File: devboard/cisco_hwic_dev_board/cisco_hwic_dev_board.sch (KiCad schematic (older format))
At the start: 3 parts, among them J1 Conn_02x20_Odd_Even, J2 Conn_02x34_Top_Bottom_Cisco, J3 Conn_01x15

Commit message: Expansion connector routed.
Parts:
- J3: footprint Connector_PinHeader_2.54mm:PinHeader_1x15_P2.54mm_Vertical -> cisco_hwic_dev_board:PinHeader_1x15_P2.54mm_Vertical_Cisco; symbol Connector_Generic:Conn_01x15 -> cisco_hwic_dev_board:Conn_01x15_Cisco
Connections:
- net labels added: PC2
- wire segments 99 -> 114
- no-connect marks 11 -> 2
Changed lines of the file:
@@
 	4400 6700 4050 6700
 Wire Wire Line
-	4400 6600 4050 6600
+	4400 6500 4050 6500
 $Comp
 L power:+5V #PWR02
 U 1 1 5DE56489
-P 4050 6600
-F 0 "#PWR02" H 4050 6450 50  0001 C CNN
-F 1 "+5V" V 4050 6800 50  0000 C CNN
-F 2 "" H 4050 6600 50  0001 C CNN
-F 3 "" H 4050 6600 50  0001 C CNN
-	1    4050 6600
+P 4050 6500
+F 0 "#PWR02" H 4050 6350 50  0001 C CNN
+F 1 "+5V" V 4050 6700 50  0000 C CNN
+F 2 "" H 4050 6500 50  0001 C CNN
+F 3 "" H 4050 6500 50  0001 C CNN
+	1    4050 6500
 	0    -1   -1   0
 $EndComp
@@
 Pin_32
 $Comp
-L Connector_Generic:Conn_01x15 J3
+L cisco_hwic_dev_board:Conn_01x15_Cisco J3
 U 1 1 5DE57370
 P 4600 6200
 F 0 "J3" H 4550 7050 50  0000 L CNN
 F 1 "Conn_01x15" H 4350 5400 50  0000 L CNN
-F 2 "Connector_PinHeader_2.54mm:PinHeader_1x15_P2.54mm_Vertical" H 4600 6200 50  0001 C CNN
+F 2 "cisco_hwic_dev_board:PinHeader_1x15_P2.54mm_Vertical_Cisco" H 4600 6200 50  0001 C CNN
 F 3 "~" H 4600 6200 50  0001 C CNN
 	1    4600 6200
@@
 	4150 5150 5000 5150
 Wire Wire Line
-	4150 5150 4150 6800
+	4150 5150 4150 6600
 Text Label 3000 2650 2    50   ~ 0
 DATA0
@@
 Wire Wire Line
 	5000 1750 5000 1850
-Wire Wire Line
-	4850 3150 5300 3150
 Text Label 5150 3150 0    50   ~ 0
 Pin_50
@@
 NoConn ~ 4400 5500
 NoConn ~ 4400 5600
-NoConn ~ 4400 5700
-NoConn ~ 4400 5800
-NoConn ~ 4400 5900
-NoConn ~ 4400 6000
-NoConn ~ 4400 6100
-NoConn ~ 4400 6200
-NoConn ~ 4400 6300
-NoConn ~ 4400 6400
-NoConn ~ 4400 6500
 Wire Wire Line
 	3400 1850 4350 1850
@@
 PA0
 Wire Wire Line
-	7650 1600 8600 1600
-Text Label 8250 1600 2    50   ~ 0
+	9100 1500 10050 1500
+Text Label 9700 1500 2    50   ~ 0
 PA1
+Wire Wire Line
+	9100 1600 10050 1600
 Text Label 8250 1700 2    50   ~ 0
-PB0
+PB2
 Wire Wire Line
 	7650 1700 8600 1700
+Text Label 9700 1700 2    50   ~ 0
+PB3
+Wire Wire Line
+	9100 1700 10050 1700
 Text Label 8250 1800 2    50   ~ 0
-PB1
+PB4
 Wire Wire Line
 	7650 1800 8600 1800
+Text Label 9700 1800 2    50   ~ 0
+PB5
+Wire Wire Line
+	9100 1800 10050 1800
 Text Label 8250 1900 2    50   ~ 0
-PB2
+PB6
 Wire Wire Line
 	7650 1900 8600 1900
+Text Label 9700 1900 2    50   ~ 0
+PB7
+Wire Wire Line
+	9100 1900 10050 1900
 Text Label 8250 2000 2    50   ~ 0
-PB3
+PB8
 Wire Wire Line
 	7650 2000 8600 2000
-Text Label 8250 2100 2    50   ~ 0
-PB4
+Wire Wire Line
+	7650 2300 8600 2300
+Text Label 8250 2300 2    50   ~ 0
+PD0
+Text Label 9700 2300 2    50   ~ 0
+PD1
+Wire Wire Line
+	7650 2400 8600 2400
+Text Label 8250 2400 2    50   ~ 0
+PD2
+Text Label 9700 2400 2    50   ~ 0
+PD3
+Wire Wire Line
+	7650 2500 8600 2500
+Text Label 8250 2500 2    50   ~ 0
+PD4
+Text Label 9700 2500 2    50   ~ 0
+PD5
+Wire Wire Line
+	7650 2600 8600 2600
+Text Label 8250 2600 2    50   ~ 0
+PD6
+Text Label 9700 2600 2    50   ~ 0
+PD7
 Wire Wire Line
 	7650 2100 8600 2100
-Text Label 8250 2200 2    50   ~ 0
-PB5
-Wire Wire Line
-	7650 2200 8600 2200
-Text Label 8250 2300 2    50   ~ 0
-PB6
-Wire Wire Line
-	7650 2300 8600 2300
-Text Label 8250 2400 2    50   ~ 0
-PB7
-Wire Wire Line
-	7650 2400 8600 2400
-Text Label 8250 2500 2    50   ~ 0
-PB8
-Wire Wire Line
-	7650 2500 8600 2500
+Text Label 8100 2100 0    50   ~ 0
+PC0
+Wire Wire Line
+	9100 2100 10050 2100
+Text Label 9550 2100 0    50   ~ 0
+PC1
+Wire Wire Line
+	7650 2800 8600 2800
+Text Label 8100 2800 0    50   ~ 0
+PG0
+Text Label 9550 2800 0    50   ~ 0
+PG1
+Wire Wire Line
+	7650 2900 8600 2900
+Text Label 8100 2900 0    50   ~ 0
+PG2
+Text Label 9550 2900 0    50   ~ 0
+PG3
+Wire Wire Line
+	7650 3000 8600 3000
+Text Label 8100 3000 0    50   ~ 0
+PG4
+Text Label 9550 3000 0    50   ~ 0
+PG5
+Wire Wire Line
+	7650 3100 8600 3100
+Text Label 8100 3100 0    50   ~ 0
+PG6
+Text Label 9550 3100 0    50   ~ 0
+PG7
+Text Label 8100 2700 0    50   ~ 0
+PE0
+Wire Wire Line
+	9100 2700 10050 2700
+Text Label 9550 2700 0    50   ~ 0
+PF0
+Wire Wire Line
+	7650 3200 8600 3200
+Text Label 8100 3200 0    50   ~ 0
+PH0
+Text Label 9550 3200 0    50   ~ 0
+PH1
 Wire Wire Line
 	7650 2700 8600 2700
-Text Label 8250 2700 2    50   ~ 0
-PD0
-Wire Wire Line
-	7650 2800 8600 2800
-Text Label 8250 2800 2    50   ~ 0
-PD1
-Wire Wire Line
-	7650 2900 8600 2900
-Text Label 8250 2900 2    50   ~ 0
-PD2
-Wire Wire Line
-	7650 3000 8600 3000
-Text Label 8250 3000 2    50   ~ 0
-PD3
-Wire Wire Line
-	7650 3100 8600 3100
-Text Label 8250 3100 2    50   ~ 0
-PD4
-Wire Wire Line
-	7650 3200 8600 3200
-Text Label 8250 3200 2    50   ~ 0
-PD5
-Wire Wire Line
-	7650 3300 8600 3300
-Text Label 8250 3300 2    50   ~ 0
-PD6
-Wire Wire Line
-	7650 3400 8600 3400
-Text Label 8250 3400 2    50   ~ 0
-PD7
-Wire Wire Line
-	9100 1600 10250 1600
-Text Label 9600 1600 0    50   ~ 0
-PC0
-Wire Wire Line
-	9100 1700 10250 1700
-Text Label 9600 1700 0    50   ~ 0
-PC1
-Wire Wire Line
-	9100 2200 10250 2200
-Text Label 9600 2200 0    50   ~ 0
-PG0
-Wire Wire Line
-	9100 2300 10250 2300
-Text Label 9600 2300 0    50   ~ 0
-PG1
-Wire Wire Line
-	9100 2400 10250 2400
-Text Label 9600 2400 0    50   ~ 0
-PG2
-Wire Wire Line
-	9100 2500 10250 2500
-Text Label 9600 2500 0    50   ~ 0
-PG3
-Wire Wire Line
-	9100 2600 10250 2600
-Text Label 9600 2600 0    50   ~ 0
-PG4
-Wire Wire Line
-	9100 2700 10250 2700
-Text Label 9600 2700 0    50   ~ 0
-PG5
-Wire Wire Line
-	9100 2800 10250 2800
-Text Label 9600 2800 0    50   ~ 0
-PG6
-Wire Wire Line
-	9100 2900 10250 2900
-Text Label 9600 2900 0    50   ~ 0
-PG7
-Text Label 9600 1800 0    50   ~ 0
-PE0
-Wire Wire Line
-	9100 1900 10250 1900
-Text Label 9600 1900 0    50   ~ 0
-PF0
-Wire Wire Line
-	9100 2000 10250 2000
-Text Label 9600 2000 0    50   ~ 0
-PH0
-Wire Wire Line
-	9100 2100 10250 2100
-Text Label 9600 2100 0    50   ~ 0
-PH1
-Wire Wire Line
-	9100 1800 10250 1800
 Wire Wire Line
 	5000 2550 5000 5150
@@
 	1    0    0    -1
 $EndComp
+Text Label 9700 1600 2    50   ~ 0
+PB1
+Wire Wire Line
+	7650 1600 8600 1600
+Text Label 8250 1600 2    50   ~ 0
+PB0
+$Comp
+L power:GND #PWR0101
+U 1 1 5DF48442
+P 9450 3700
+F 0 "#PWR0101" H 9450 3450 50  0001 C CNN
+F 1 "GND" H 9455 3527 50  0000 C CNN
+F 2 "" H 9450 3700 50  0001 C CNN
+F 3 "" H 9450 3700 50  0001 C CNN
+	1    9450 3700
+	1    0    0    -1
+$EndComp
+Wire Wire Line
+	9450 2000 9100 2000
+$Comp
+L power:+3.3V #PWR0102
+U 1 1 5DF5771D
+P 10050 3400
+F 0 "#PWR0102" H 10050 3250 50  0001 C CNN
+F 1 "+3.3V" V 10065 3528 50  0000 L CNN
+F 2 "" H 10050 3400 50  0001 C CNN
+F 3 "" H 10050 3400 50  0001 C CNN
+	1    10050 3400
+	0    1    1    0
+$EndComp
+$Comp
+L power:+5V #PWR0103
+U 1 1 5DF5945C
+P 7650 3400
+F 0 "#PWR0103" H 7650 3250 50  0001 C CNN
+F 1 "+5V" V 7665 3528 50  0000 L CNN
+F 2 "" H 7650 3400 50  0001 C CNN
+F 3 "" H 7650 3400 50  0001 C CNN
+	1    7650 3400
+	0    -1   -1   0
+$EndComp
+Wire Wire Line
+	9100 3400 10050 3400
+Wire Wire Line
+	8600 3400 7650 3400
+Wire Wire Line
+	4400 6600 4150 6600
+Connection ~ 4150 6600
+Wire Wire Line
+	4150 6600 4150 6800
+Text Label 6000 3150 0    50   ~ 0
+PC2
+Wire Wire Line
+	4850 3150 6000 3150
+Wire Wire Line
+	7650 2200 8600 2200
+Text Label 8100 2200 0    50   ~ 0
+PC2
+Wire Wire Line
+	9450 2000 9450 2200
+Wire Wire Line
+	9100 3200 10050 3200
+Wire Wire Line
+	9100 3100 10050 3100
+Wire Wire Line
+	9100 3000 10050 3000
+Wire Wire Line
+	9100 2900 10050 2900
+Wire Wire Line
+	9100 2800 10050 2800
+Wire Wire Line
+	9100 2600 10050 2600
+Wire Wire Line
+	9100 2500 10050 2500
+Wire Wire Line
+	9100 2400 10050 2400
+Wire Wire Line
+	9100 2300 10050 2300
+Wire Wire Line
+	9450 2200 9100 2200
+Connection ~ 9450 2200
+Wire Wire Line
+	9450 2200 9450 3300
+Wire Wire Line
+	9100 3300 9450 3300
+Connection ~ 9450 3300
+Wire Wire Line
+	9450 3300 9450 3550
+Wire Wire Line
+	8600 3300 8450 3300
+Wire Wire Line
+	8450 3300 8450 3550
+Wire Wire Line
+	8450 3550 9450 3550
+Connection ~ 9450 3550
+Wire Wire Line
+	9450 3550 9450 3700
 $EndSCHEMATC

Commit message: First version.
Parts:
- added C1, C2: C, Capacitor_SMD:C_0603_1608Metric_Pad1.05x0.95mm_HandSolder, symbol Device:C
- added J4: USB Blaster Active Serial, Connector_PinHeader_2.54mm:PinHeader_2x05_P2.54mm_Vertical, symbol Connector_Generic:Conn_02x05_Odd_Even
- added J5: ATT85_VIN, Connector_PinHeader_2.54mm:PinHeader_1x01_P2.54mm_Vertical, symbol Connector_Generic:Conn_01x01
- added J6: SD Card, Connector_PinHeader_2.54mm:PinHeader_1x06_P2.54mm_Vertical, symbol Connector_Generic:Conn_01x06
- added J7: Power, Connector_PinHeader_2.54mm:PinHeader_1x03_P2.54mm_Horizontal, symbol Connector_Generic:Conn_01x03
- added JP1: 3.3V Main, Connector_PinHeader_2.54mm:PinHeader_2x01_P2.54mm_Vertical, symbol Jumper:Jumper_2_Bridged
- added JP2: Jumper_3_Bridged12, Connector_PinHeader_2.54mm:PinHeader_1x03_P2.54mm_Vertical, symbol Jumper:Jumper_3_Bridged12
- added R3, R4, R5, R6, R7, R8: NS, Resistor_SMD:R_0603_1608Metric_Pad1.05x0.95mm_HandSolder, symbol Device:R
- added U1: AT25xxx, Package_SO:SOIC-8_3.9x4.9mm_P1.27mm, symbol Memory_EEPROM:AT25xxx
- added U2: ATtiny85_devboard, cisco_hwic_dev_board:Digispark_ATtiny85, symbol cisco_hwic_dev_board:ATtiny85_devboard
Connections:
- net labels added: SD_CSN, SPISD_CSN, SPI_CK, SPI_CSN, SPI_MISO, SPI_MOSI, UB_ASDI, UB_CONF_DONE, UB_DATAOUT, UB_DCLK, UB_nCE, UB_nCONFIG, UB_nCS
- wire segments 114 -> 176
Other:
- note added: "3.3V is connected to 5V: the ATtiny85 is 5V powered\nwhen it’s plugged into the USB port, but it’s 3.3V \npowered on this board, because all IO voltage levels \nare 3.3V as well.\nThis jumper must be open when the ATtiny85 board\nis plugged in, but the USB connecter is powered."
- note added: "This pin can be used to power the ATtiny with a voltage\nlarger than 5V because it goes to a 5V regular.\nIf you do this, make sure to open the 3.3V Main jumper\nbelow, otherwise you’ll feed 5V to logic that expect 3.3V."
- moved on the sheet: J1, J2, J3

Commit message: Various fixes after broken rev 1.
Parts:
- J1: footprint Connector_PinSocket_2.54mm:PinSocket_2x20_P2.54mm_Horizontal -> Connector_PinHeader_2.54mm:PinHeader_2x20_P2.54mm_Vertical
- U1: footprint Package_SO:SOIC-8_3.9x4.9mm_P1.27mm -> Package_SO:SOIC-8_5.275x5.275mm_P1.27mm
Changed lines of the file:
@@
 F 0 "J1" H 7100 2817 50  0000 C CNN
 F 1 "Conn_02x20_Odd_Even" H 7100 2726 50  0000 C CNN
-F 2 "Connector_PinSocket_2.54mm:PinSocket_2x20_P2.54mm_Horizontal" H 7050 1700 50  0001 C CNN
+F 2 "Connector_PinHeader_2.54mm:PinHeader_2x20_P2.54mm_Vertical" H 7050 1700 50  0001 C CNN
 F 3 "~" H 7050 1700 50  0001 C CNN
 	1    7050 1700
@@
 F 0 "U1" H 5600 5850 50  0000 C CNN
 F 1 "AT25xxx" H 5700 5250 50  0000 C CNN
-F 2 "Package_SO:SOIC-8_3.9x4.9mm_P1.27mm" H 5500 5550 50  0001 C CNN
+F 2 "Package_SO:SOIC-8_5.275x5.275mm_P1.27mm" H 5500 5550 50  0001 C CNN
 F 3 "http://ww1.microchip.com/downloads/en/DeviceDoc/Atmel-8707-SEEPROM-AT25010B-020B-040B-Datasheet.pdf" H 5500 5550 50  0001 C CNN
 	1    5500 5550

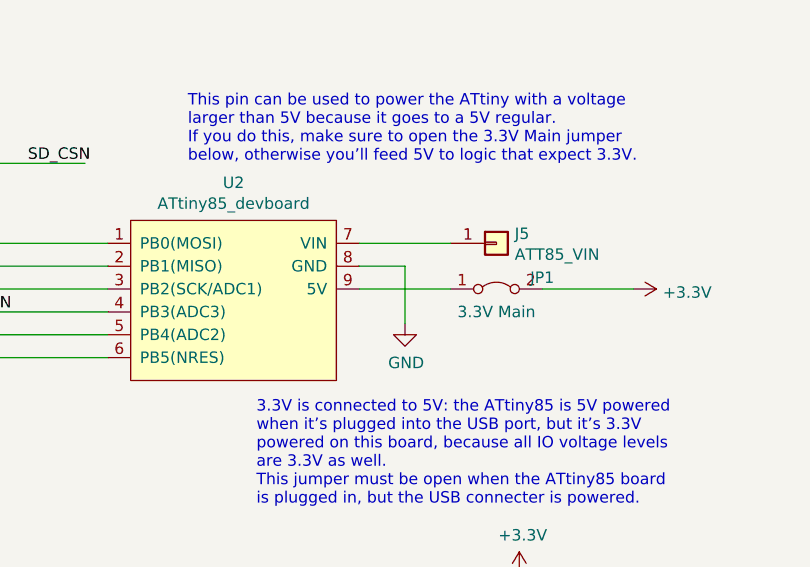
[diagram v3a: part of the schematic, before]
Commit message: Move ATtiny and SDcard for accessibility while soldered down.
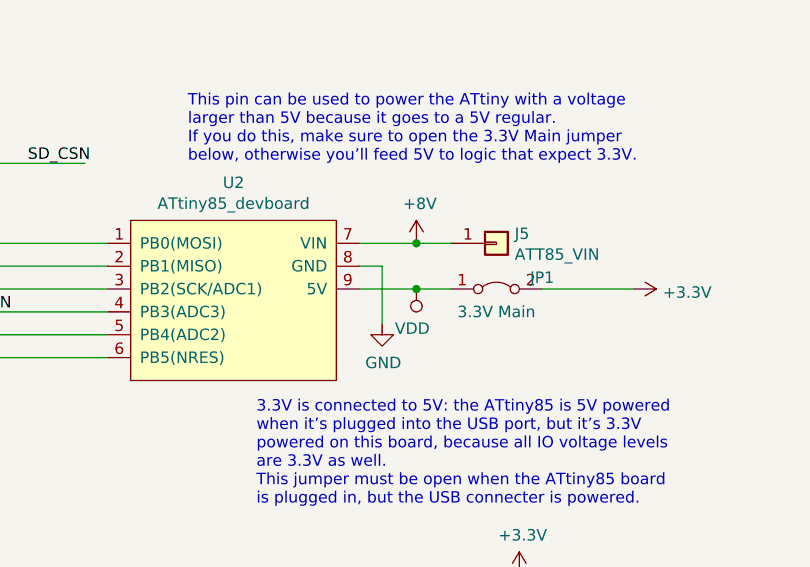
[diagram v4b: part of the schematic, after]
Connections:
- net labels added: +8V, VDD
- wire segments 176 -> 178
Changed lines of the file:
@@
 $EndComp
 Wire Wire Line
-	9700 3950 9500 3950
-Wire Wire Line
-	9700 3950 9700 4200
+	9600 3950 9500 3950
+Wire Wire Line
+	9600 3950 9600 4200
 $Comp
 L power:GND #PWR09
 U 1 1 5DF16041
-P 9700 4200
-F 0 "#PWR09" H 9700 3950 50  0001 C CNN
-F 1 "GND" H 9705 4027 50  0000 C CNN
-F 2 "" H 9700 4200 50  0001 C CNN
-F 3 "" H 9700 4200 50  0001 C CNN
-	1    9700 4200
-	1    0    0    -1
-$EndComp
-Wire Wire Line
-	9500 4050 9900 4050
-Wire Wire Line
-	9500 3850 9900 3850
+P 9600 4200
+F 0 "#PWR09" H 9600 3950 50  0001 C CNN
+F 1 "GND" H 9605 4027 50  0000 C CNN
+F 2 "" H 9600 4200 50  0001 C CNN
+F 3 "" H 9600 4200 50  0001 C CNN
+	1    9600 4200
+	1    0    0    -1
+$EndComp
+Wire Wire Line
+	9500 4050 9750 4050
+Wire Wire Line
+	9500 3850 9750 3850
 $Comp
 L Jumper:Jumper_2_Bridged JP1
@@
 	0    -1   -1   0
 $EndComp
+$Comp
+L power:+8V #PWR?
+U 1 1 5DFC2108
+P 9750 3850
+F 0 "#PWR?" H 9750 3700 50  0001 C CNN
+F 1 "+8V" H 9765 4023 50  0000 C CNN
+F 2 "" H 9750 3850 50  0001 C CNN
+F 3 "" H 9750 3850 50  0001 C CNN
+	1    9750 3850
+	1    0    0    -1
+$EndComp
+Connection ~ 9750 3850
+Wire Wire Line
+	9750 3850 9900 3850
+$Comp
+L power:VDD #PWR?
+U 1 1 5DFC2F08
+P 9750 4050
+F 0 "#PWR?" H 9750 3900 50  0001 C CNN
+F 1 "VDD" H 9768 4223 50  0000 C CNN
+F 2 "" H 9750 4050 50  0001 C CNN
+F 3 "" H 9750 4050 50  0001 C CNN
+	1    9750 4050
+	-1   0    0    1
+$EndComp
+Connection ~ 9750 4050
+Wire Wire Line
+	9750 4050 9900 4050
 $EndSCHEMATC
